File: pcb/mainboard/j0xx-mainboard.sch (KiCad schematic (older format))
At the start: 20 parts, among them J1 USB_C_Receptacle, Q1 BSS138, SW1 reset, U1 ATmega32U4-AU, Y1 Resonator

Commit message: wip
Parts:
- added C7: 0.1u, Capacitor_SMD:C_0805_2012Metric, symbol Device:C
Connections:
- net +5V: now also C7.1
- net GND: now also C7.2
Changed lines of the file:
@@
 Wire Wire Line
 	6850 1250 6950 1250
+Wire Wire Line
+	7150 1250 7350 1250
+Wire Wire Line
+	7350 1250 7350 1200
+Wire Wire Line
+	7350 850  7150 850
+Wire Wire Line
+	7350 900  7350 850
+$Comp
+L Device:C C7
+U 1 1 611BEE24
+P 7350 1050
+F 0 "C7" H 7350 1150 50  0000 L CNN
+F 1 "0.1u" H 7350 950 50  0000 L CNN
+F 2 "Capacitor_SMD:C_0805_2012Metric" H 7388 900 50  0001 C CNN
+F 3 "~" H 7350 1050 50  0001 C CNN
+	1    7350 1050
+	1    0    0    -1
+$EndComp
 $EndSCHEMATC

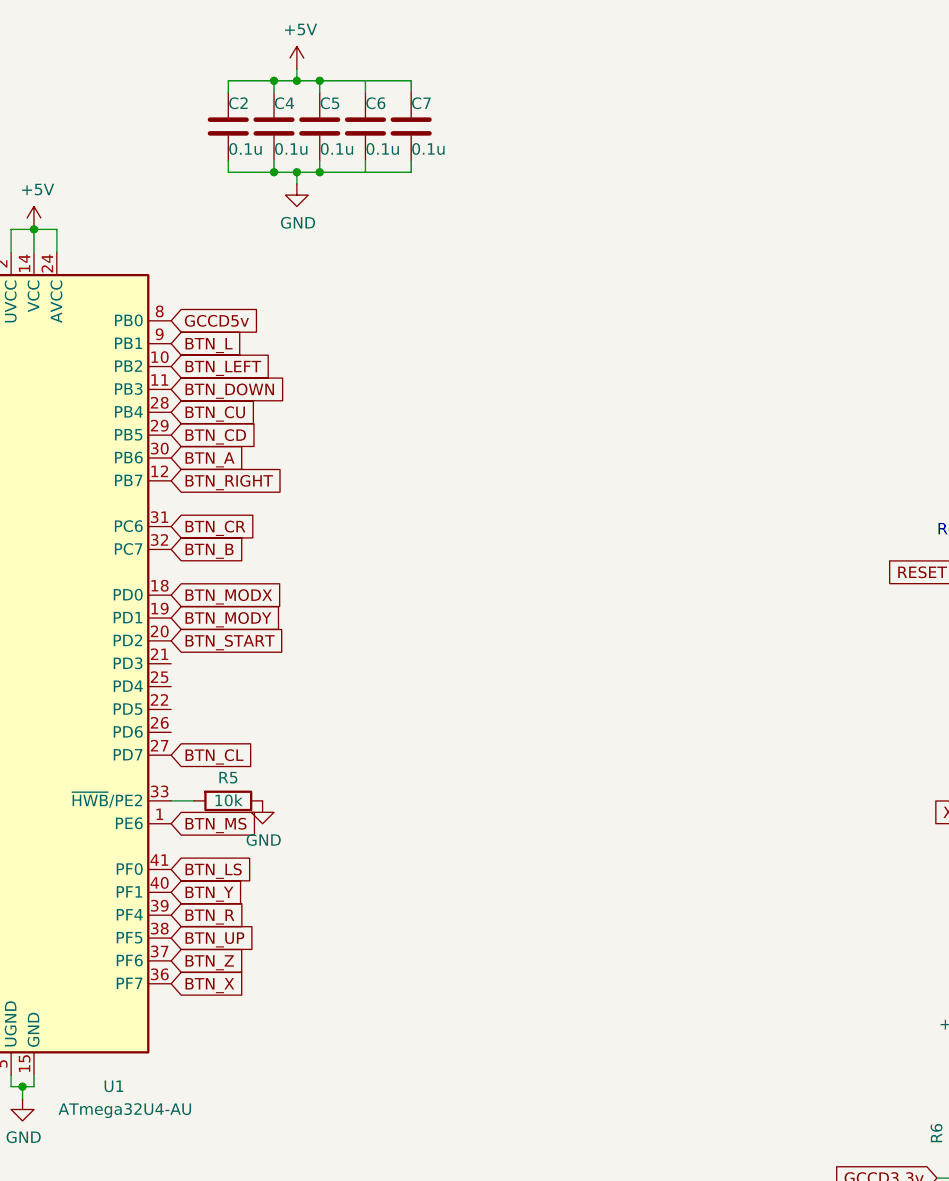
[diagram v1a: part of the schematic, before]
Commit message: rearrange parts, add connectors and outline
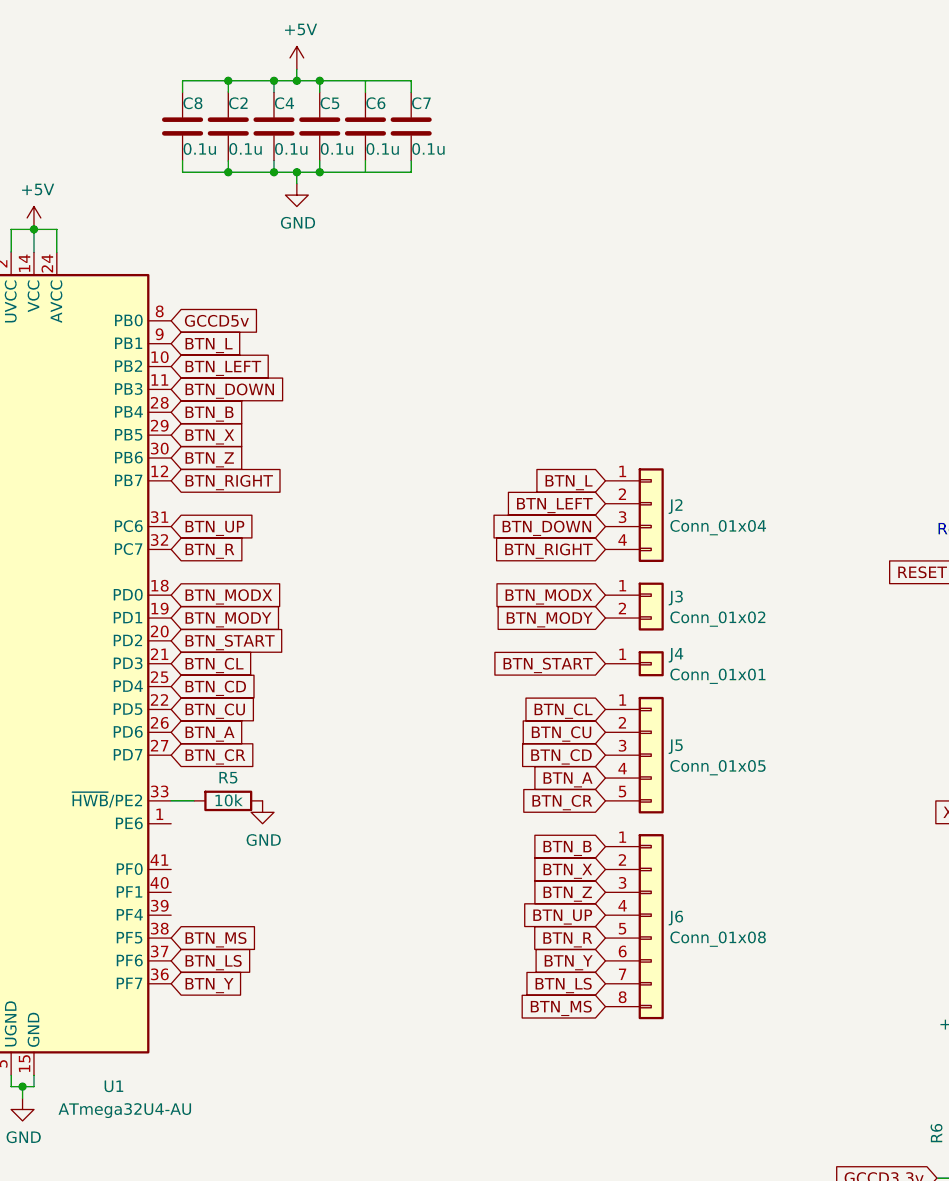
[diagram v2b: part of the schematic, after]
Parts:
- added C8: 0.1u, Capacitor_SMD:C_0805_2012Metric, symbol Device:C
- added J2: Conn_01x04, Connector_PinHeader_2.54mm:PinHeader_1x04_P2.54mm_Vertical, symbol Connector_Generic:Conn_01x04
- added J3: Conn_01x02, Connector_PinHeader_2.54mm:PinHeader_1x02_P2.54mm_Vertical, symbol Connector_Generic:Conn_01x02
- added J4: Conn_01x01, Connector_PinHeader_2.54mm:PinHeader_1x01_P2.54mm_Vertical, symbol Connector_Generic:Conn_01x01
- added J5: Conn_01x05, Connector_PinHeader_2.54mm:PinHeader_1x05_P2.54mm_Vertical, symbol Connector_Generic:Conn_01x05
- added J6: Conn_01x08, Connector_PinHeader_2.54mm:PinHeader_1x08_P2.54mm_Vertical, symbol Connector_Generic:Conn_01x08
- U1: footprint Package_DFN_QFN:QFN-44-1EP_7x7mm_P0.5mm_EP5.2x5.2mm -> Package_QFP:TQFP-44_10x10mm_P0.8mm
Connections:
- net +5V: now also C8.1
- net BTN_A: now also U1.26 (PD6), J5.4 (Pin_4); no longer U1.30 (PB6)
- net BTN_B: now also U1.28 (PB4), J6.1 (Pin_1); no longer U1.32 (PC7)
- net BTN_CD: now also U1.25 (PD4), J5.3 (Pin_3); no longer U1.29 (PB5)
- net BTN_CL: now also U1.21 (PD3), J5.1 (Pin_1); no longer U1.27 (PD7)
- net BTN_CR: now also U1.27 (PD7), J5.5 (Pin_5); no longer U1.31 (PC6)
- net BTN_CU: now also U1.22 (PD5), J5.2 (Pin_2); no longer U1.28 (PB4)
- net BTN_DOWN: now also J2.3 (Pin_3)
- net BTN_L: now also J2.1 (Pin_1)
- net BTN_LEFT: now also J2.2 (Pin_2)
- net BTN_LS: now also U1.37 (PF6), J6.7 (Pin_7); no longer U1.41 (PF0)
- net BTN_MODX: now also J3.1 (Pin_1)
- net BTN_MODY: now also J3.2 (Pin_2)
- net BTN_MS: now also U1.38 (PF5), J6.8 (Pin_8); no longer U1.1 (PE6)
- net BTN_R: now also U1.32 (PC7), J6.5 (Pin_5); no longer U1.39 (PF4)
- net BTN_RIGHT: now also J2.4 (Pin_4)
- net BTN_START: now also J4.1 (Pin_1)
- net BTN_UP: now also U1.31 (PC6), J6.4 (Pin_4); no longer U1.38 (PF5)
- net BTN_X: now also U1.29 (PB5), J6.2 (Pin_2); no longer U1.36 (PF7)
- net BTN_Y: now also U1.36 (PF7), J6.6 (Pin_6); no longer U1.40 (PF1)
- net BTN_Z: now also U1.30 (PB6), J6.3 (Pin_3); no longer U1.37 (PF6)
- net GND: now also C8.2
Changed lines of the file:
@@
 F 0 "U1" H 6050 1550 50  0000 C CNN
 F 1 "ATmega32U4-AU" H 6100 1450 50  0000 C CNN
-F 2 "Package_DFN_QFN:QFN-44-1EP_7x7mm_P0.5mm_EP5.2x5.2mm" H 5700 3400 50  0001 C CIN
+F 2 "Package_QFP:TQFP-44_10x10mm_P0.8mm" H 5700 3400 50  0001 C CIN
 F 3 "http://ww1.microchip.com/downloads/en/DeviceDoc/Atmel-7766-8-bit-AVR-ATmega16U4-32U4_Datasheet.pdf" H 5700 3400 50  0001 C CNN
 F 4 "C112161" H 5700 3400 50  0001 C CNN "LCSC"
@@
 NoConn ~ 2000 3500
 NoConn ~ 2000 3600
-Text GLabel 6300 4500 2    50   Input ~ 0
+Text GLabel 6300 2900 2    50   Input ~ 0
 BTN_R
-Text GLabel 6300 4400 2    50   Input ~ 0
+Text GLabel 6300 4800 2    50   Input ~ 0
 BTN_Y
-Text GLabel 6300 4300 2    50   Input ~ 0
+Text GLabel 6300 4700 2    50   Input ~ 0
 BTN_LS
-Text GLabel 6300 4100 2    50   Input ~ 0
+Text GLabel 6300 4600 2    50   Input ~ 0
 BTN_MS
-Text GLabel 6300 2900 2    50   Input ~ 0
+Text GLabel 6300 2300 2    50   Input ~ 0
 BTN_B
-Text GLabel 6300 4800 2    50   Input ~ 0
+Text GLabel 6300 2400 2    50   Input ~ 0
 BTN_X
-Text GLabel 6300 4700 2    50   Input ~ 0
+Text GLabel 6300 2500 2    50   Input ~ 0
 BTN_Z
+Text GLabel 6300 3400 2    50   Input ~ 0
+BTN_CL
+Text GLabel 6300 3600 2    50   Input ~ 0
+BTN_CU
+Text GLabel 6300 3500 2    50   Input ~ 0
+BTN_CD
+Text GLabel 6300 3700 2    50   Input ~ 0
+BTN_A
 Text GLabel 6300 3800 2    50   Input ~ 0
-BTN_CL
-Text GLabel 6300 2300 2    50   Input ~ 0
-BTN_CU
-Text GLabel 6300 2400 2    50   Input ~ 0
-BTN_CD
-Text GLabel 6300 2500 2    50   Input ~ 0
-BTN_A
-Text GLabel 6300 2800 2    50   Input ~ 0
 BTN_CR
 Text GLabel 6300 2600 2    50   Input ~ 0
@@
 Text GLabel 6300 3300 2    50   Input ~ 0
 BTN_START
-Text GLabel 6300 4600 2    50   Input ~ 0
+Text GLabel 6300 2800 2    50   Input ~ 0
 BTN_UP
 Text GLabel 6300 3100 2    50   Input ~ 0
@@
 	6850 1300 6850 1250
 $Comp
-L power:GND #PWR?
+L power:GND #PWR0101
 U 1 1 611B39FF
 P 6850 1300
-F 0 "#PWR?" H 6850 1050 50  0001 C CNN
+F 0 "#PWR0101" H 6850 1050 50  0001 C CNN
 F 1 "GND" H 6855 1127 50  0000 C CNN
 F 2 "" H 6850 1300 50  0001 C CNN
@@
 $EndComp
 $Comp
-L power:+5V #PWR?
+L power:+5V #PWR0102
 U 1 1 611C5E81
 P 5700 1500
-F 0 "#PWR?" H 5700 1350 50  0001 C CNN
+F 0 "#PWR0102" H 5700 1350 50  0001 C CNN
 F 1 "+5V" H 5715 1673 50  0000 C CNN
 F 2 "" H 5700 1500 50  0001 C CNN
@@
 	1    0    0    -1
 $EndComp
+Wire Wire Line
+	6350 1250 6550 1250
+Wire Wire Line
+	6350 1250 6350 1200
+Wire Wire Line
+	6550 850  6350 850
+Wire Wire Line
+	6350 900  6350 850
+$Comp
+L Device:C C8
+U 1 1 61237907
+P 6350 1050
+F 0 "C8" H 6350 1150 50  0000 L CNN
+F 1 "0.1u" H 6350 950 50  0000 L CNN
+F 2 "Capacitor_SMD:C_0805_2012Metric" H 6388 900 50  0001 C CNN
+F 3 "~" H 6350 1050 50  0001 C CNN
+	1    6350 1050
+	1    0    0    -1
+$EndComp
+Connection ~ 6550 850
+Connection ~ 6550 1250
+$Comp
+L Connector_Generic:Conn_01x01 J4
+U 1 1 612408C6
+P 8400 3400
+F 0 "J4" H 8480 3442 50  0000 L CNN
+F 1 "Conn_01x01" H 8480 3351 50  0000 L CNN
+F 2 "Connector_PinHeader_2.54mm:PinHeader_1x01_P2.54mm_Vertical" H 8400 3400 50  0001 C CNN
+F 3 "~" H 8400 3400 50  0001 C CNN
+	1    8400 3400
+	1    0    0    -1
+$EndComp
+Text GLabel 8200 3400 0    50   Input ~ 0
+BTN_START
+$Comp
+L Connector_Generic:Conn_01x02 J3
+U 1 1 612419D3
+P 8400 3100
+F 0 "J3" H 8480 3092 50  0000 L CNN
+F 1 "Conn_01x02" H 8480 3001 50  0000 L CNN
+F 2 "Connector_PinHeader_2.54mm:PinHeader_1x02_P2.54mm_Vertical" H 8400 3100 50  0001 C CNN
+F 3 "~" H 8400 3100 50  0001 C CNN
+	1    8400 3100
+	1    0    0    -1
+$EndComp
+$Comp
+L Connector_Generic:Conn_01x05 J5
+U 1 1 61243789
+P 8400 3800
+F 0 "J5" H 8480 3842 50  0000 L CNN
+F 1 "Conn_01x05" H 8480 3751 50  0000 L CNN
+F 2 "Connector_PinHeader_2.54mm:PinHeader_1x05_P2.54mm_Vertical" H 8400 3800 50  0001 C CNN
+F 3 "~" H 8400 3800 50  0001 C CNN
+	1    8400 3800
+	1    0    0    -1
+$EndComp
+$Comp
+L Connector_Generic:Conn_01x08 J6
+U 1 1 61244495
+P 8400 4500
+F 0 "J6" H 8480 4492 50  0000 L CNN
+F 1 "Conn_01x08" H 8480 4401 50  0000 L CNN
+F 2 "Connector_PinHeader_2.54mm:PinHeader_1x08_P2.54mm_Vertical" H 8400 4500 50  0001 C CNN
+F 3 "~" H 8400 4500 50  0001 C CNN
+	1    8400 4500
+	1    0    0    -1
+$EndComp
+$Comp
+L Connector_Generic:Conn_01x04 J2
+U 1 1 6124D075
+P 8400 2700
+F 0 "J2" H 8480 2692 50  0000 L CNN
+F 1 "Conn_01x04" H 8480 2601 50  0000 L CNN
+F 2 "Connector_PinHeader_2.54mm:PinHeader_1x04_P2.54mm_Vertical" H 8400 2700 50  0001 C CNN
+F 3 "~" H 8400 2700 50  0001 C CNN
+	1    8400 2700
+	1    0    0    -1
+$EndComp
+Text GLabel 8200 2600 0    50   Input ~ 0
+BTN_L
+Text GLabel 8200 2700 0    50   Input ~ 0
+BTN_LEFT
+Text GLabel 8200 2800 0    50   Input ~ 0
+BTN_DOWN
+Text GLabel 8200 2900 0    50   Input ~ 0
+BTN_RIGHT
+Text GLabel 8200 3100 0    50   Input ~ 0
+BTN_MODX
+Text GLabel 8200 3200 0    50   Input ~ 0
+BTN_MODY
+Text GLabel 8200 3600 0    50   Input ~ 0
+BTN_CL
+Text GLabel 8200 3700 0    50   Input ~ 0
+BTN_CU
+Text GLabel 8200 3800 0    50   Input ~ 0
+BTN_CD
+Text GLabel 8200 3900 0    50   Input ~ 0
+BTN_A
+Text GLabel 8200 4000 0    50   Input ~ 0
+BTN_CR
+Text GLabel 8200 4200 0    50   Input ~ 0
+BTN_B
+Text GLabel 8200 4300 0    50   Input ~ 0
+BTN_X
+Text GLabel 8200 4400 0    50   Input ~ 0
+BTN_Z
+Text GLabel 8200 4500 0    50   Input ~ 0
+BTN_UP
+Text GLabel 8200 4600 0    50   Input ~ 0
+BTN_R
+Text GLabel 8200 4700 0    50   Input ~ 0
+BTN_Y
+Text GLabel 8200 4800 0    50   Input ~ 0
+BTN_LS
+Text GLabel 8200 4900 0    50   Input ~ 0
+BTN_MS
 $EndSCHEMATC
